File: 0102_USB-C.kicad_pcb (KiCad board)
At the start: 2 copper layers, 42 x 25 mm, 11 parts, among them J1 UPSTREAM, J2 DOWNSTREAM, SW1 EN

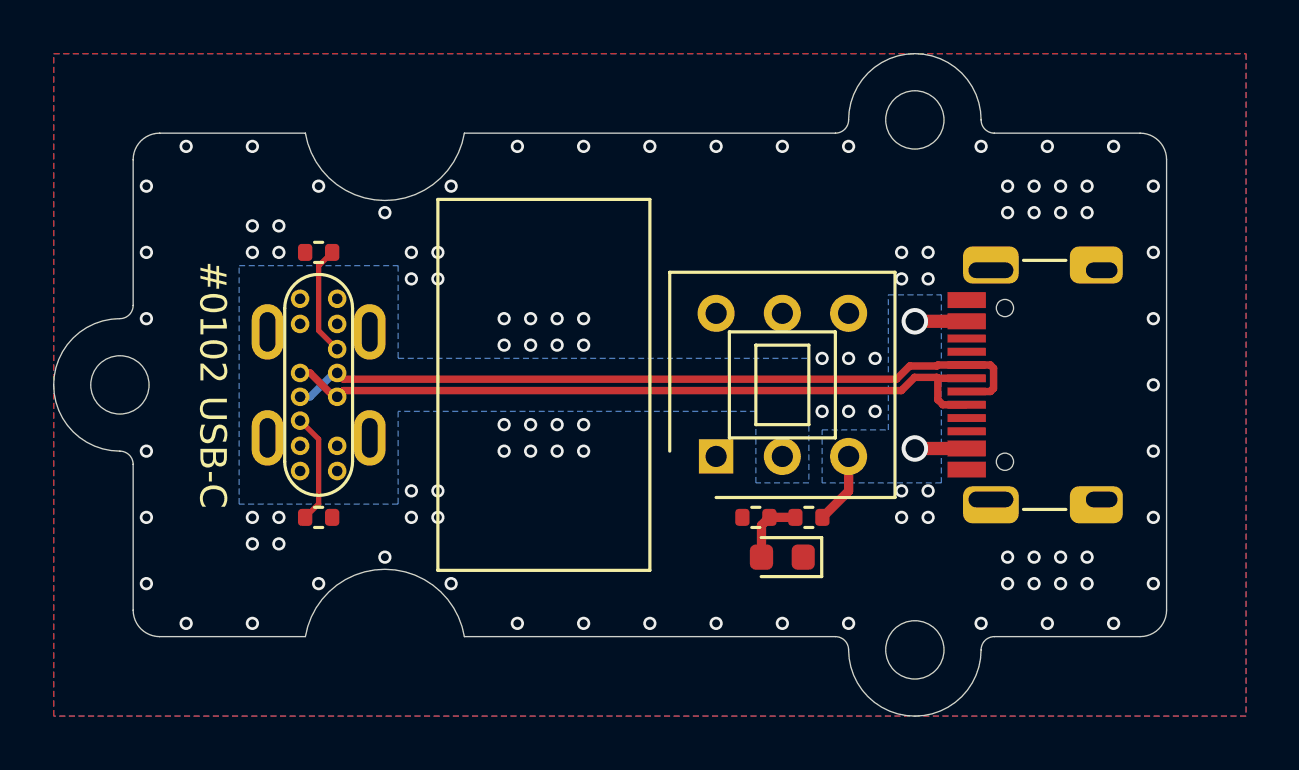
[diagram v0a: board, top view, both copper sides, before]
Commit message: Rework USB-C for stand Type-A downstream
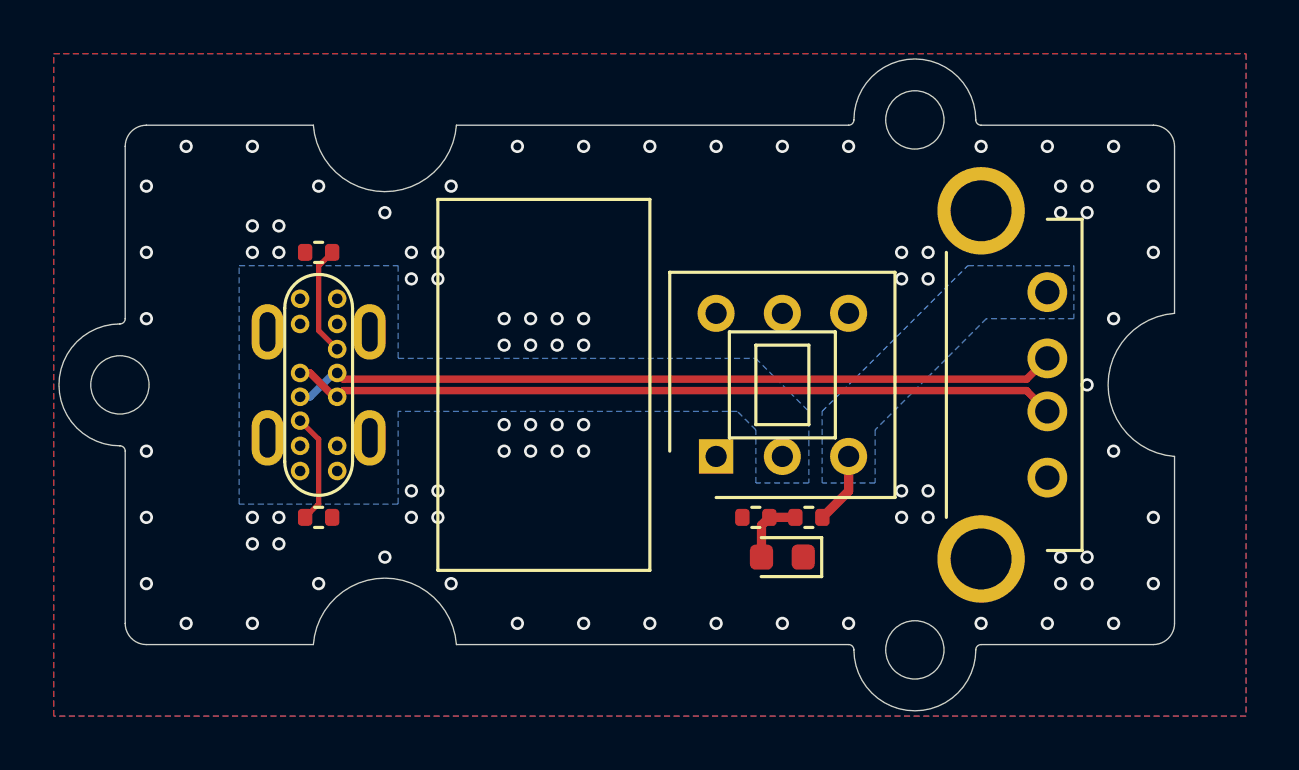
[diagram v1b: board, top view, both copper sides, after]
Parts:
- J2: footprint JLC-SMT:HRO_TYPE-C-31-M-12 -> JLC-SMT:CKMTW_USBAS04P
- moved J2 1.00 mm to (135.0, 110.0), turned to 270 degrees
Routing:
- net /VOUT: track 6.62 -> 2.71 mm, vias 2 -> 0
- net /D-: track 27.8 -> 29.0 mm
- net GND: vias 103 -> 89
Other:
- board size 42 x 25 mm -> 42.1 x 24.6 mm
- board text removed: "#0102 USB-C"

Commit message: Output gerber for USB-C V1.0
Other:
- board text added: "#0102 USB-C V1.0"
- board text added: "JLCJLCJLCJLC"
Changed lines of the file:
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@@
   (general
     (thickness 1.2)
-    (drawings 51)
+    (drawings 53)
     (tracks 112)
     (zones 0)
@@
     (pad_to_mask_clearance 0.05)
     (solder_mask_min_width 0.1)
-    (aux_axis_origin 0 0)
+    (aux_axis_origin 97.7 122.3)
     (grid_origin 100 100)
     (visible_elements FFFFFF7F)
@@
     )
   )
+  (gr_text JLCJLCJLCJLC (at 118 102 180) (layer B.SilkS)
+    (effects (font (size 0.8 0.8) (thickness 0.12)) (justify left mirror))
+  )
+  (gr_text "#0102 USB-C\nV1.0" (at 118 110 180) (layer B.SilkS)
+    (effects (font (size 1 1) (thickness 0.15)) (justify left mirror))
+  )
   (gr_arc (start 140 110) (end 139.800001 107.300001) (angle -171.5272104) (layer Edge.Cuts) (width 0.05))

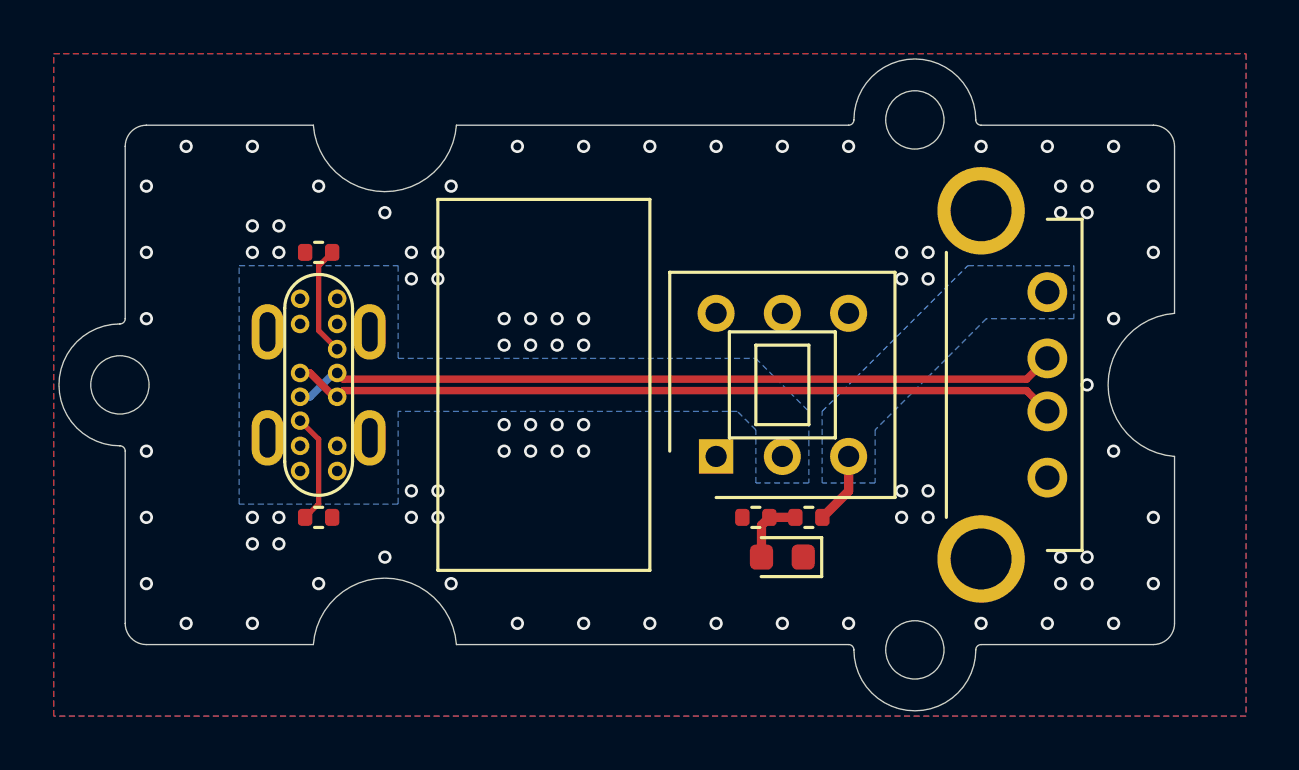
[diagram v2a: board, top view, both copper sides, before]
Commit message: Fix USB-C
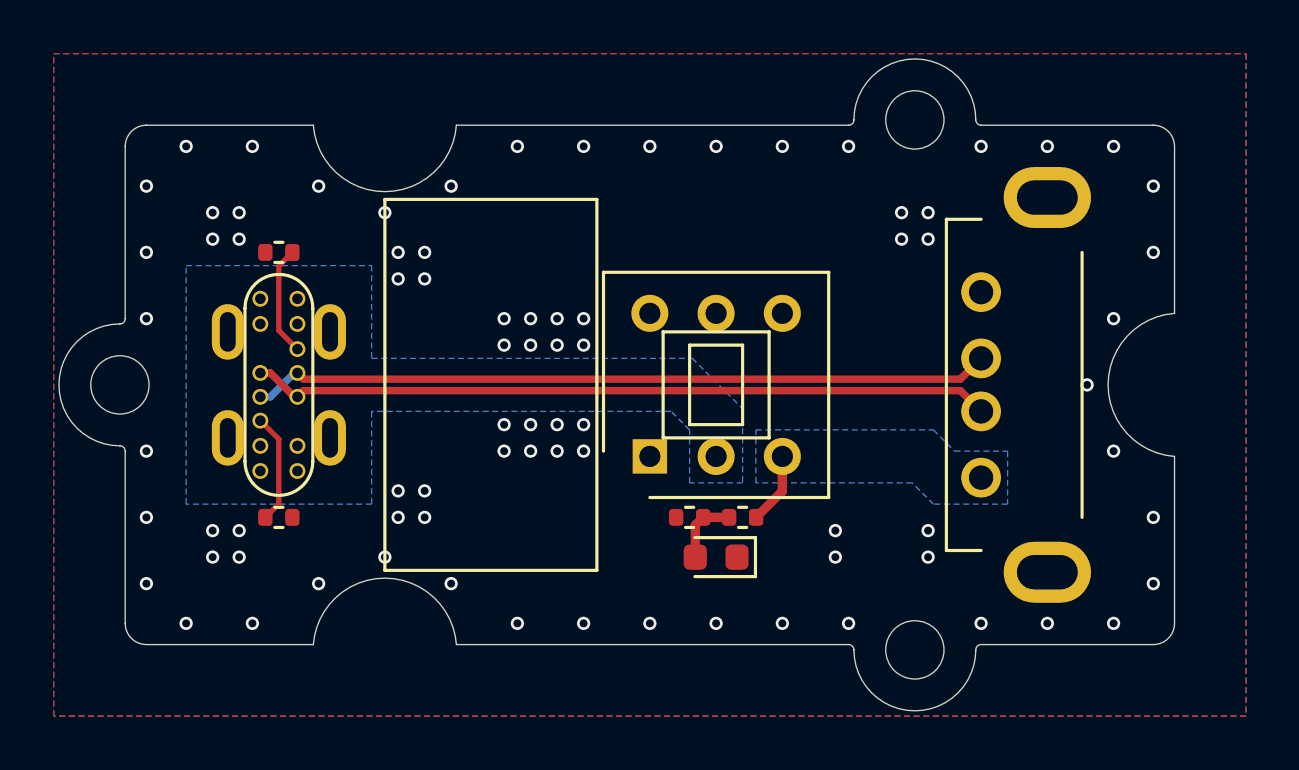
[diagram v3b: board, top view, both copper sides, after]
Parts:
- R1: value 22.1K -> 2K
- R2: value 47.5K -> NC
- moved D1 2.50 mm to (122.5, 116.5)
- moved J2 2.50 mm to (132.5, 110.0), turned to 90 degrees
- moved R1 2.50 mm to (123.5, 115.0)
- moved R2 2.50 mm to (121.5, 115.0)
- moved SW1 2.50 mm to (122.5, 110.0)
- moved J1 1.50 mm to (106.0, 110.0)
- moved R3 1.50 mm to (106.0, 115.0)
- moved R4 1.50 mm to (106.0, 105.0)
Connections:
- J2 pad 2: /D+ -> /D-
- J2 pad 3: /D- -> /D+
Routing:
- net /D-: track 29.0 -> 28.0 mm
- net /D+: track 29.0 -> 28.0 mm
- net GND: vias 89 -> 81
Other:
- board text added: "#0102 USB-C V1.1"
- board text removed: "#0102 USB-C V1.0"
